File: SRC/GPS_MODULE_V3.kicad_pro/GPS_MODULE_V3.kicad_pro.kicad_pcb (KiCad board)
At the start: 4 copper layers, 50.1 x 41 mm, 141 parts, among them J1 Input, J3 nano_sim, J4 Micro_SD_Card, J5 Conn_02x06_Counter_Clockwise, Q1 SSM3J328R-HXY, Q2 BSN20, Q3 BSN20, Q4 2N7002, Q5 2N7002, Q6 2N7002, Q7 2N7002, U1 SY8089AAAC, U2 STM32F103C8Tx, U3 A9G_MODULE, U4 MAX485E, U5 XC6206PxxxMR, U7 ATA6561-GAQW-N, U8 W25Q32JVSS, Y1 8MHz, Y2 32.678KHz

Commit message: completed GPS ecoboda files
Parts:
- removed H2: MountingHole, MountingHole:MountingHole_2.7mm
- removed J1: Input, TerminalBlock_Phoenix:TerminalBlock_Phoenix_PT-1,5-2-3.5-H_1x02_P3.50mm_Horizontal
- removed R33, R36, R45, R50: 1K, Resistor_SMD:R_0402_1005Metric
- added AE3: Antenna_Shield, greencharge-footprints:UFL_COAX_CONN23370191, B.Cu at (230.9, 72.4)
- added C19: 0.1u, Capacitor_SMD:C_0402_1005Metric, B.Cu at (234.6, 82.8)
- added FL1: SAFEB1G57KE0F00R15, Filter:Filter_1411-5_1.4x1.1mm, B.Cu at (235.5, 69.5)
- added R51: 0R, Resistor_SMD:R_0402_1005Metric, B.Cu at (264.3, 72.8)
- AE1: footprint greencharge-footprints:UFL_COAX_CONN23370191 -> Connector_Coaxial:SMA_Samtec_SMA-J-P-X-ST-EM1_EdgeMount
- C23, R17: moved to F.Cu
- C24, C25, C26, C27, U5: moved to B.Cu
- D2, D3, D4: value SS310 -> RS1K-E3/5AT
- D5, D8, D9: footprint LED_SMD:LED_0603_1608Metric -> LED_SMD:LED_0402_1005Metric
- moved C27 46.9 mm to (229.1, 96.8), turned to 0 degrees
- moved C26 45.3 mm to (229.1, 95.6), turned to 0 degrees
- moved U5 41.1 mm to (229.5, 93.0), turned to 90 degrees
- moved C24 40.5 mm to (226.1, 91.8), turned to -90 degrees
- moved C25 39.0 mm to (227.2, 91.8), turned to -90 degrees
- moved G*** 35.0 mm to (261.3, 81.5)
- moved D6 28.0 mm to (263.8, 71.3), turned to 0 degrees
- moved R7 18.2 mm to (243.2, 67.8)
- moved D5 17.6 mm to (242.1, 67.8)
- moved G*** 10.6 mm to (270.2, 87.3)
- moved AE2 8.03 mm to (264.3, 67.7), turned to 180 degrees
- moved AE1 7.93 mm to (225.5, 73.9), turned to 90 degrees
- moved C20 4.39 mm to (260.0, 67.5)
- moved R17 3.87 mm to (258.7, 67.2), turned to 180 degrees
- moved C23 3.85 mm to (258.7, 68.2), turned to 180 degrees
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- renumbered J3 to JE
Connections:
- C16 pad 1: +5V -> /5V_FILTERED_
- C38 pad 1: +5V -> /5V_FILTERED_
- C6 pad 1: +5V -> /5V_FILTERED_
- D2 pad 2: +5V -> /5V_FILTERED_
- D6 pad 2: Net-(AE1-A) -> Net-(AE2-A)
- L3 pad 1: GND -> Net-(AE1-A)
- L3 pad 2: Net-(AE1-A) -> 4.2V_SIMPWR
- Q1 pad 3: +5V -> /5V_FILTERED_
- Q4 pad 2: Net-(Q4-S) -> /A9G_GSM_GPRS_MODULE/MOSFET_LOGIC_LEVEL_TRANSLATOR9/LOW_SIDE_LOGIC_SIGNAL
- Q5 pad 2: Net-(Q5-S) -> /A9G_GSM_GPRS_MODULE/MOSFET_LOGIC_LEVEL_TRANSLATOR6/LOW_SIDE_LOGIC_SIGNAL
- Q6 pad 2: Net-(Q6-S) -> /A9G_GSM_GPRS_MODULE/MOSFET_LOGIC_LEVEL_TRANSLATOR7/LOW_SIDE_LOGIC_SIGNAL
- Q7 pad 2: Net-(Q7-S) -> /A9G_GSM_GPRS_MODULE/MOSFET_LOGIC_LEVEL_TRANSLATOR8/LOW_SIDE_LOGIC_SIGNAL
- R30 pad 2: Net-(Q4-S) -> /A9G_GSM_GPRS_MODULE/MOSFET_LOGIC_LEVEL_TRANSLATOR9/LOW_SIDE_LOGIC_SIGNAL
- R34 pad 2: Net-(Q5-S) -> /A9G_GSM_GPRS_MODULE/MOSFET_LOGIC_LEVEL_TRANSLATOR6/LOW_SIDE_LOGIC_SIGNAL
- R43 pad 2: Net-(Q6-S) -> /A9G_GSM_GPRS_MODULE/MOSFET_LOGIC_LEVEL_TRANSLATOR7/LOW_SIDE_LOGIC_SIGNAL
- R48 pad 2: Net-(Q7-S) -> /A9G_GSM_GPRS_MODULE/MOSFET_LOGIC_LEVEL_TRANSLATOR8/LOW_SIDE_LOGIC_SIGNAL
- TH1 pad 1: Net-(J1-Pin_1) -> +5V
- U1 pad 1: +5V -> /5V_FILTERED_
- U1 pad 4: +5V -> /5V_FILTERED_
- U2 pad 32: /CAN_TRANSCEIVER_ATA6561/CAN_TX -> /CAN_TRANSCEIVER_ATA6561/CAN_RX
- U2 pad 33: /CAN_TRANSCEIVER_ATA6561/CAN_RX -> /CAN_TRANSCEIVER_ATA6561/CAN_TX
- U3 pad 28: Net-(AE1-A) -> Net-(U3-GPS_RF)
- U3 pad 45: Net-(AE2-A) -> Net-(U3-GSM_RF)
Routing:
- net Net-(D5-K): track 4.00 -> 39.8 mm, vias 0 -> 2
- net 4.2V_SIMPWR: track 33.9 -> 59.1 mm, vias 6 -> 8
- net /STM32F103C8T6_MCU/3v3_stm: track 66.9 -> 86.4 mm
- net /RS485_MAX485/B: track 21.0 -> 34.1 mm
- net Net-(U3-GSM_RF): track 0.00 -> 7.82 mm
- net /5V_FILTERED_: track 0.00 -> 7.37 mm, vias 0 -> 22
- net GND: track 102.1 -> 109.2 mm, vias 253 -> 462
- net Net-(Q4-S): track 6.74 -> 0.00 mm, vias 2 -> 0
- net B_to_CANH: track 36.9 -> 43.5 mm
- net Net-(AE1-A): track 6.82 -> 13.3 mm
- net /RS485_MAX485/A: track 28.4 -> 34.2 mm
- net /A9G_GSM_GPRS_MODULE/MOSFET_LOGIC_LEVEL_TRANSLATOR8/LOW_SIDE_LOGIC_SIGNAL: track 21.2 -> 26.3 mm
- net Net-(Q5-S): track 4.78 -> 0.00 mm
- net /A9G_GSM_GPRS_MODULE/MOSFET_LOGIC_LEVEL_TRANSLATOR6/LOW_SIDE_LOGIC_SIGNAL: track 44.1 -> 48.8 mm
- net Net-(U3-GPS_RF): track 0.00 -> 4.58 mm
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- added copper zone on B.Cu, net /5V_FILTERED_
- added copper zone on F.Cu, net /5V_FILTERED_
- added copper zone on In2.Cu, net /5V_FILTERED_
- removed copper zone on B.Cu, net +5V
- removed copper zone on F.Cu, net +5V
- removed copper zone on In2.Cu, net +5V
- removed copper zone on B.Cu, net Net-(J1-Pin_1)
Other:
- board text added: "3V3"
- board text removed: "+3V3"

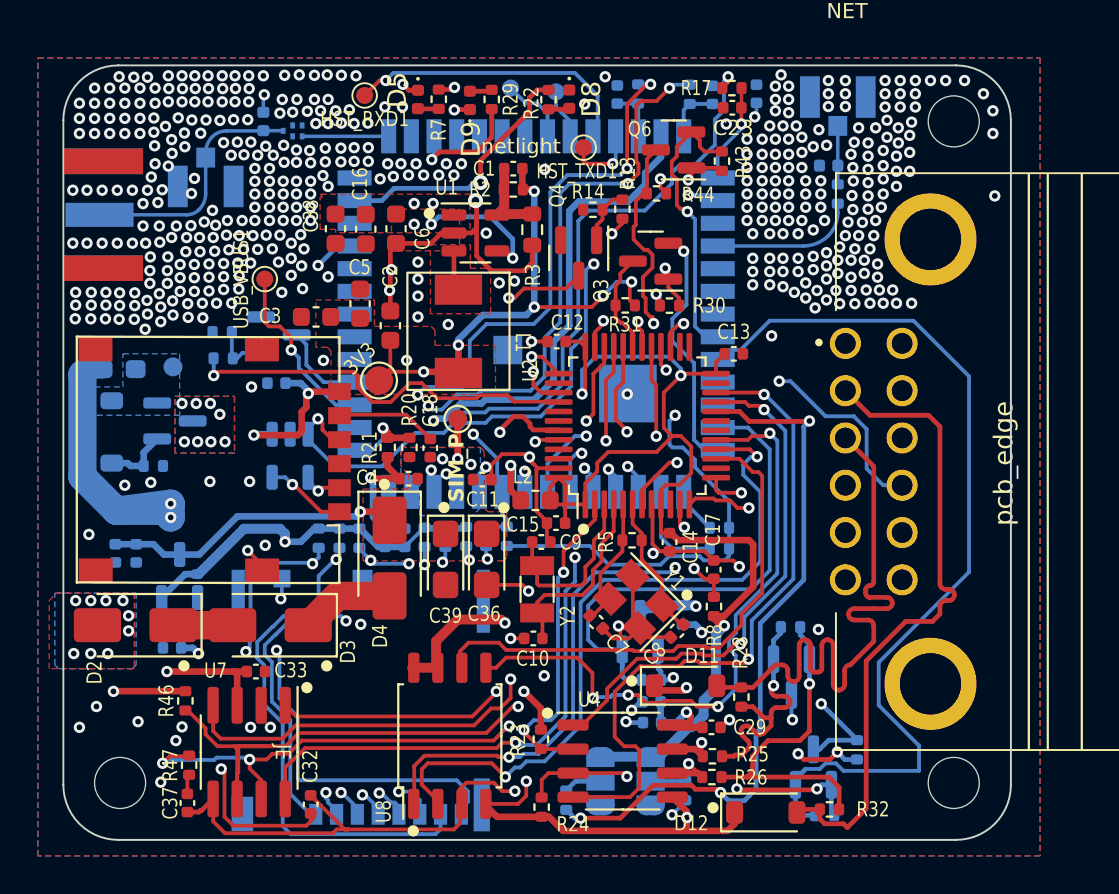
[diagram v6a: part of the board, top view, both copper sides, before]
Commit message: update removal of all level shifts diodes
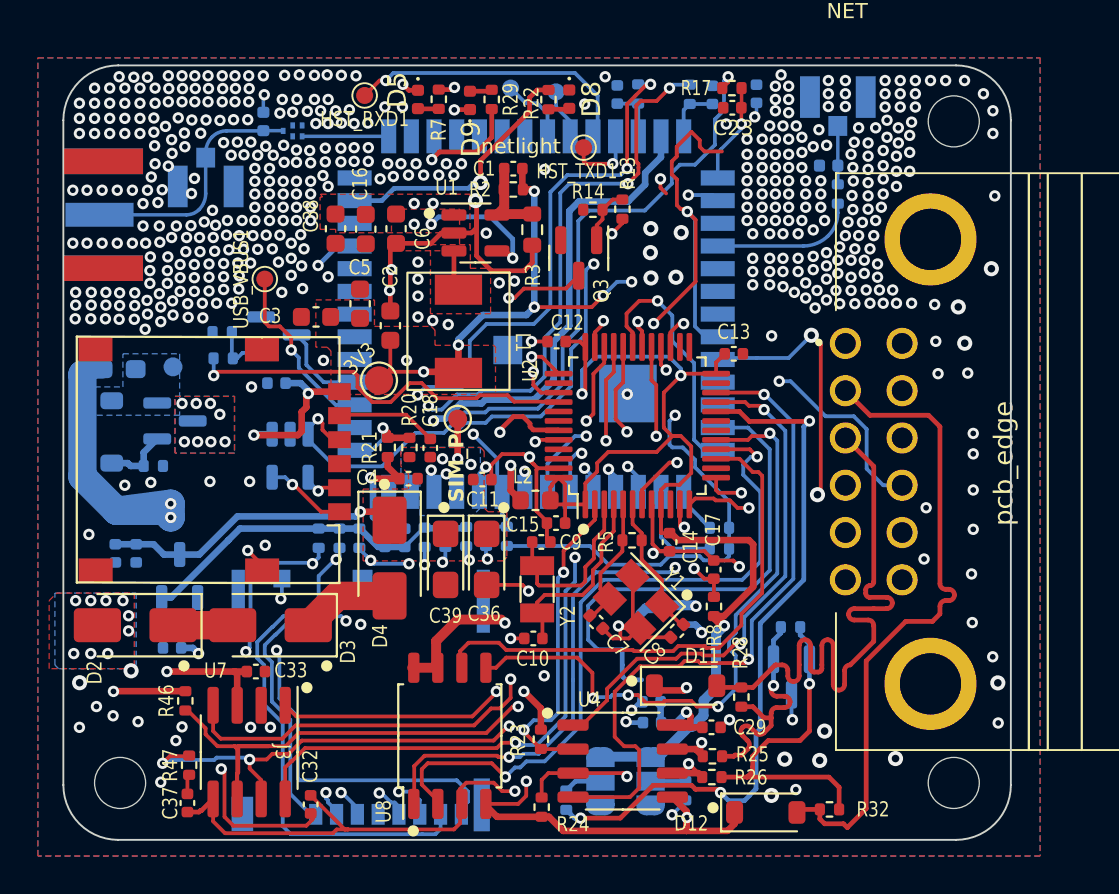
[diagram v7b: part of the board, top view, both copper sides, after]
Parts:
- removed Q4, Q5, Q6, Q7: 2N7002, Package_TO_SOT_SMD:SOT-23
- removed R30, R31, R34, R35, R43, R44, R48, R49: 10K, Resistor_SMD:R_0402_1005Metric
- renumbered JE to J3
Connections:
- U3 pad 49: /A9G_GSM_GPRS_MODULE/MOSFET_LOGIC_LEVEL_TRANSLATOR7/LOW_SIDE_LOGIC_SIGNAL -> /STM32F103C8T6_MCU/TX2
- U3 pad 50: /A9G_GSM_GPRS_MODULE/MOSFET_LOGIC_LEVEL_TRANSLATOR6/LOW_SIDE_LOGIC_SIGNAL -> /STM32F103C8T6_MCU/RX2
- U3 pad 53: /A9G_GSM_GPRS_MODULE/MOSFET_LOGIC_LEVEL_TRANSLATOR8/LOW_SIDE_LOGIC_SIGNAL -> /STM32F103C8T6_MCU/TX1
- U3 pad 54: /A9G_GSM_GPRS_MODULE/MOSFET_LOGIC_LEVEL_TRANSLATOR9/LOW_SIDE_LOGIC_SIGNAL -> /STM32F103C8T6_MCU/RX1
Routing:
- net 2V8: track 147.7 -> 21.0 mm, vias 8 -> 0
- net /A9G_GSM_GPRS_MODULE/MOSFET_LOGIC_LEVEL_TRANSLATOR6/LOW_SIDE_LOGIC_SIGNAL: track 48.8 -> 0.00 mm
- net /A9G_GSM_GPRS_MODULE/MOSFET_LOGIC_LEVEL_TRANSLATOR8/LOW_SIDE_LOGIC_SIGNAL: track 26.3 -> 0.00 mm
- net /STM32F103C8T6_MCU/TX1: track 33.6 -> 59.9 mm
- net /A9G_GSM_GPRS_MODULE/MOSFET_LOGIC_LEVEL_TRANSLATOR9/LOW_SIDE_LOGIC_SIGNAL: track 17.4 -> 0.00 mm, vias 2 -> 0
- net /A9G_GSM_GPRS_MODULE/MOSFET_LOGIC_LEVEL_TRANSLATOR7/LOW_SIDE_LOGIC_SIGNAL: track 15.0 -> 0.00 mm, vias 1 -> 0
- net /STM32F103C8T6_MCU/TX2: track 29.0 -> 40.2 mm, vias 2 -> 3
- net +3V3: track 129.9 -> 118.9 mm, vias 15 -> 13
- net /STM32F103C8T6_MCU/RX1: track 5.37 -> 13.4 mm, vias 0 -> 1
- net /STM32F103C8T6_MCU/RX2: track 21.0 -> 20.3 mm, vias 2 -> 3
- net GND: vias 462 -> 495

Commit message: GPS all files BOM and placemnt guide files added
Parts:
- removed AE3: Antenna_Shield, greencharge-footprints:UFL_COAX_CONN23370191
- removed R32: 0R, Resistor_SMD:R_0402_1005Metric
- added C35: 100n, Capacitor_SMD:C_0402_1005Metric, B.Cu at (139.8, 89.6)
- added C40: C_Small, Capacitor_SMD:C_0402_1005Metric, B.Cu at (166.9, 82.2)
- added C41: C_Small, Capacitor_SMD:C_0402_1005Metric, B.Cu at (166.9, 79.4)
- added L5: L_Ferrite, Inductor_SMD:L_0402_1005Metric, F.Cu at (161.3, 109.8)
- added L6: L_Ferrite, Inductor_SMD:L_0402_1005Metric, F.Cu at (163.0, 112.3)
- AE1: footprint Connector_Coaxial:SMA_Samtec_SMA-J-P-X-ST-EM1_EdgeMount -> Connector_Coaxial:SMA_Molex_73251-2200_Horizontal
- C38: footprint Capacitor_SMD:C_0603_1608Metric -> Capacitor_SMD:C_0402_1005Metric
- G***: moved to F.Cu
- L2: footprint Inductor_SMD:L_0603_1608Metric -> Inductor_SMD:L_0402_1005Metric
- R28: value 0R -> 22R; moved to B.Cu
- TH1: footprint Fuse:Fuse_0603_1608Metric_Pad1.05x0.95mm_HandSolder -> Fuse:Fuse_1206_3216Metric
- TP2: footprint TestPoint:TestPoint_Pad_D1.5mm -> TestPoint:TestPoint_Pad_D1.0mm
- moved R28 121.8 mm to (139.8, 75.0)
- moved C16 98.8 mm to (140.9, 82.5)
- moved C6 98.8 mm to (142.5, 82.5)
- moved G*** 98.7 mm to (163.5, 94.0)
- moved C13 98.6 mm to (160.5, 88.7), turned to 90 degrees
- moved C23 98.2 mm to (160.8, 76.1)
- moved D10 98.2 mm to (163.9, 106.2)
- moved J5 98.2 mm to (182.4, 94.8)
- moved C12 98.2 mm to (151.5, 88.4)
- moved C14 98.2 mm to (157.5, 99.0)
- moved C15 98.2 mm to (151.5, 98.0)
- moved C17 98.2 mm to (159.8, 100.5)
- moved C19 98.2 mm to (136.7, 90.6)
- moved C24 98.2 mm to (128.2, 99.6)
- moved C26 98.2 mm to (131.2, 103.5)
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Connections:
- L3 pad 1: Net-(AE1-A) -> Net-(L3-Pad1)
- R28 pad 1: Net-(D10-K-Pad1) -> Net-(L3-Pad1)
- R28 pad 2: /RS485_MAX485/B -> Net-(AE1-A)
- U3 pad 49: /STM32F103C8T6_MCU/TX2 -> /STM32F103C8T6_MCU/RX2
- U3 pad 50: /STM32F103C8T6_MCU/RX2 -> /STM32F103C8T6_MCU/TX2
- U4 pad 1: /STM32F103C8T6_MCU/TX3 -> /STM32F103C8T6_MCU/RX3
- U4 pad 4: /STM32F103C8T6_MCU/RX3 -> /STM32F103C8T6_MCU/TX3
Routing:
- net /STM32F103C8T6_MCU/TX1: track 59.9 -> 18.0 mm
- net 2V8: track 21.0 -> 40.5 mm, vias 0 -> 2
- net +3V3: track 118.9 -> 104.1 mm, vias 13 -> 8
- net Net-(U3-HST_TXD): track 15.6 -> 3.23 mm
- net /STM32F103C8T6_MCU/TX2: track 40.2 -> 27.9 mm, vias 3 -> 2
- net Net-(D5-K): track 39.8 -> 31.0 mm
- net /STM32F103C8T6_MCU/TX3: track 27.6 -> 35.5 mm
- net Net-(U3-VUSB_DET): track 9.54 -> 16.6 mm
- net /STM32F103C8T6_MCU/RX3: track 35.8 -> 28.7 mm
- net 4.2V_SIMPWR: track 59.1 -> 52.7 mm
- net /A9G_GSM_GPRS_MODULE/TF_CARD_CONN/SD_CLK: track 44.5 -> 49.8 mm
- net GND: track 109.2 -> 104.2 mm, vias 495 -> 382
- net Net-(D10-K-Pad2): track 18.1 -> 13.3 mm
- net /A9G_GSM_GPRS_MODULE/TF_CARD_CONN/SD_D3: track 35.6 -> 39.8 mm
- net /A9G_GSM_GPRS_MODULE/TF_CARD_CONN/SD_D1: track 46.7 -> 50.7 mm
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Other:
- outline, holes or cut-outs redrawn
